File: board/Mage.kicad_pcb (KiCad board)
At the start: 2 copper layers, 77 x 37 mm, 26 parts, among them SW0 RESET, SW1 Up, SW2 Down, SW3 Left, SW4 Right, SW5 BTN A, SW6 BTN B, SW7 BTN C, SW8 POWER, U1 ATTiny85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

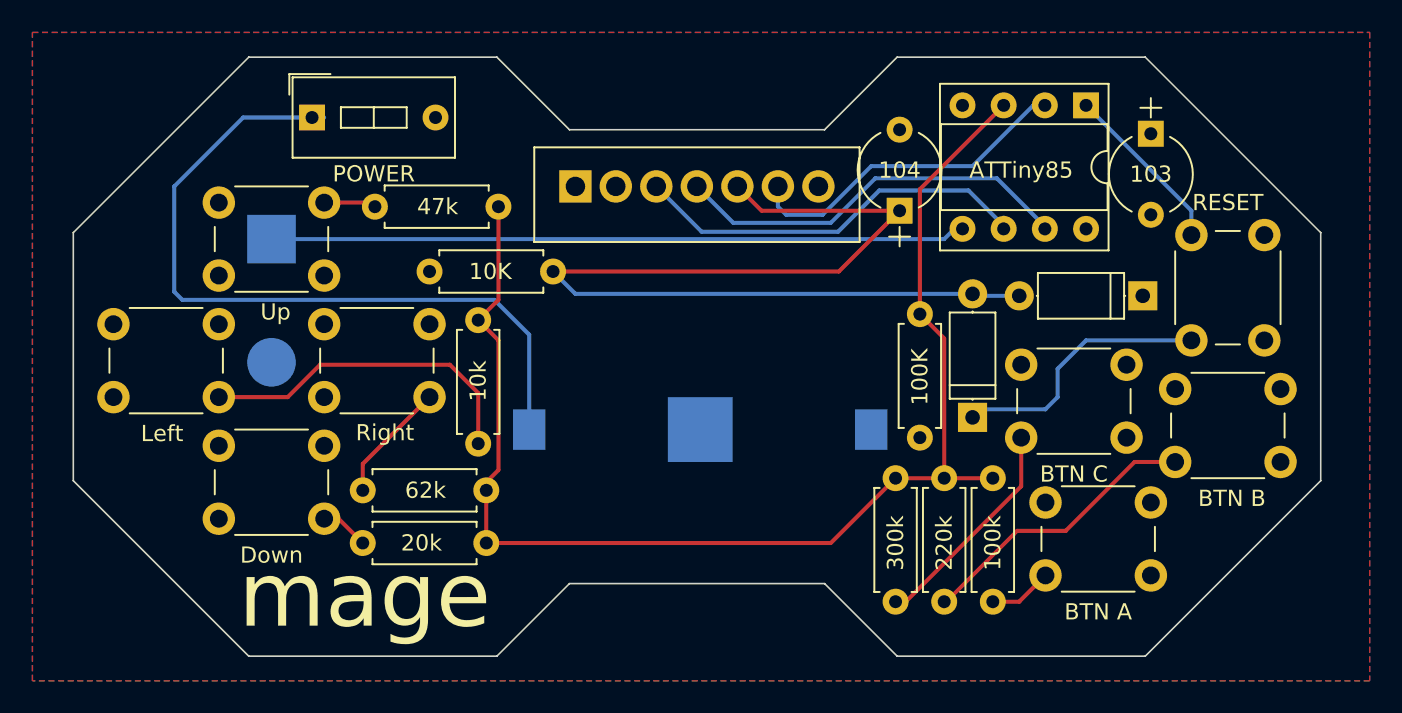
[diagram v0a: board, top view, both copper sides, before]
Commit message: reworked board to make it neater
Added decoupling capacitor for OLED
Removed CR2032, replaced with Lipo
Tweaked layout
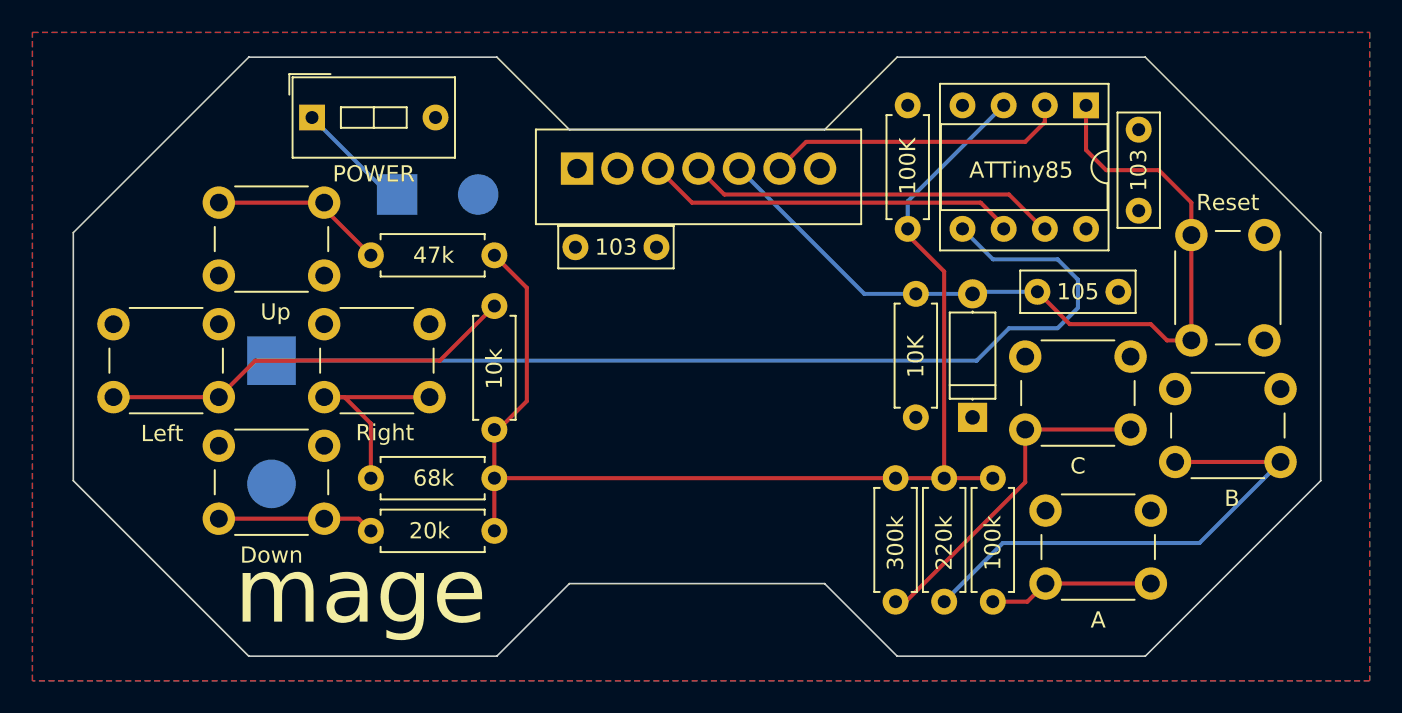
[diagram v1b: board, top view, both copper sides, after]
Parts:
- removed CR2032: Battery_Cell, Custom Footprints:3008_coin_cell
- removed D1: D_ALT, Diodes_THT:D_A-405_P7.62mm_Horizontal
- added BT1: 3.7v Lipo, Custom Footprints:LiPo_Pads, B.Cu at (145.0, 95.0)
- added C2: 103, Capacitors_THT:C_Rect_L7.0mm_W2.5mm_P5.00mm, F.Cu at (161.0, 98.2)
- C0: value 103 -> 105; footprint Capacitors_THT:CP_Radial_Tantal_D5.0mm_P5.00mm -> Capacitors_THT:C_Rect_L7.0mm_W2.5mm_P5.00mm
- C1: value 104 -> 103; footprint Capacitors_THT:CP_Radial_Tantal_D5.0mm_P5.00mm -> Capacitors_THT:C_Rect_L7.0mm_W2.5mm_P5.00mm
- R4: value 62k -> 68k
- SW0: value RESET -> Reset
- SW5: value BTN A -> A
- SW6: value BTN B -> B
- SW7: value BTN C -> C
- moved R10 31.3 mm to (182.0, 108.8), turned to 90 degrees
- moved R9 20.5 mm to (181.5, 89.5), turned to 270 degrees
- moved C1 15.6 mm to (195.8, 91.0), turned to 270 degrees
- moved C0 12.0 mm to (189.5, 101.0), turned to 0 degrees
- moved LS1 7.50 mm to (142.2, 105.2)
- moved R3 6.82 mm to (156.0, 109.5), turned to 90 degrees
- moved R1 3.01 mm to (156.0, 98.8)
- moved U2 1.10 mm to (161.1, 93.4)
- moved R2 0.90 mm to (156.0, 115.8)
- moved R4 0.90 mm to (156.0, 112.5)
- moved SW7 0.56 mm to (188.8, 105.0)
- moved SW5 0.50 mm to (190.0, 114.5)
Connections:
- C0 pad 1: GND -> Net-(C0-Pad1)
- C0 pad 2: +3V3 -> GND
- C1 pad 1: Net-(C1-Pad1) -> GND
- C1 pad 2: GND -> +3V3
- D0 pad 1: Net-(D0-Pad1) -> +3V3
- D0 pad 2: Net-(C1-Pad1) -> Net-(C0-Pad1)
- R10 pad 2: Net-(C1-Pad1) -> Net-(C0-Pad1)
- SW0 pad 2: Net-(D0-Pad1) -> Net-(C0-Pad1)
- U1 pad 1: Net-(D0-Pad1) -> Net-(C0-Pad1)
- U2 pad 5: Net-(C1-Pad1) -> Net-(C0-Pad1)
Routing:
- net Net-(C1-Pad1): track 64.3 -> 0.00 mm
- net Net-(C0-Pad1): track 0.00 -> 52.3 mm
- net Net-(BT1-Pad1): track 46.4 -> 7.22 mm
- net Net-(D0-Pad1): track 27.2 -> 0.00 mm
- net Net-(LS1-Pad1): track 42.9 -> 61.3 mm
- net Net-(R6-Pad2): track 17.8 -> 31.3 mm
- net Net-(R1-Pad2): track 3.23 -> 10.9 mm
- net Net-(R7-Pad2): track 13.7 -> 20.8 mm
- net Net-(R2-Pad2): track 3.00 -> 9.69 mm
- net Net-(R5-Pad2): track 3.92 -> 10.2 mm
- net Net-(R4-Pad2): track 7.46 -> 13.4 mm
- net Net-(R3-Pad2): track 20.7 -> 25.8 mm
- net Net-(R1-Pad1): track 80.8 -> 75.9 mm
- net Net-(U1-Pad7): track 25.5 -> 22.9 mm
- net Net-(U1-Pad6): track 25.4 -> 23.0 mm
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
